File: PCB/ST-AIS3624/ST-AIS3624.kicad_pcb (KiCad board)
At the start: 2 copper layers, 25 x 9 mm, 5 parts, among them J1 Conn_02x03_Odd_Even

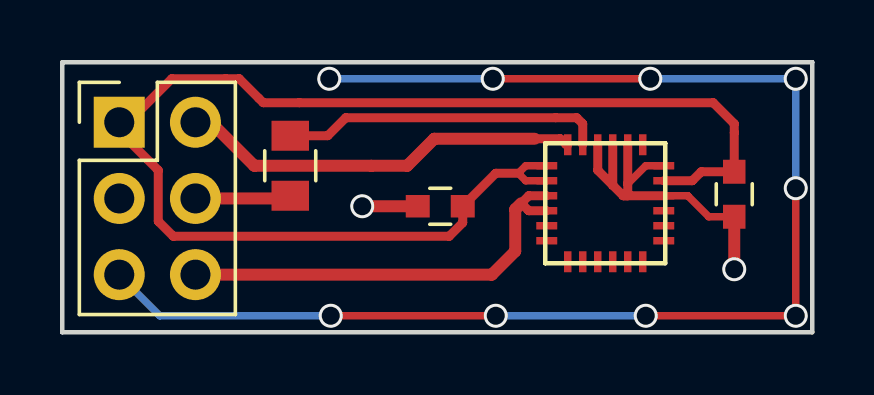
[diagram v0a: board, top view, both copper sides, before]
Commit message: PCB - AIS3624 fix  bad wiring for SPI interface 3-wire
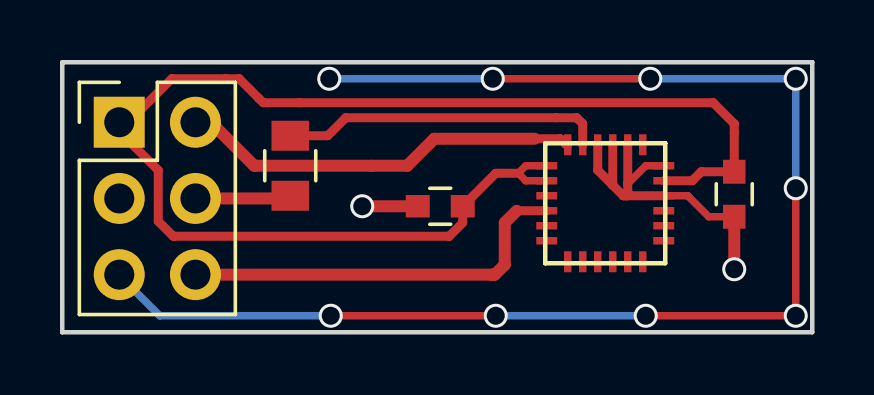
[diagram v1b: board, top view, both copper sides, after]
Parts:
- AIS36241: value Acc1 -> AIS3624DQTR
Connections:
- AIS36241 pad 15: /Miso/Mosi -> Net-(AIS36241-Pad15)
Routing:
- net /Miso/Mosi: track 14.6 -> 13.4 mm
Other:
- board text added: "BI-SDI"
- board text added: "SDO"
- board text removed: "MOSI MISO"
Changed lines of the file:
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@@
 (kicad_pcb (version 4) (host pcbnew 4.0.7)
   (general
-    (links 18)
+    (links 17)
     (no_connects 0)
-    (area 107.214287 61.8 150.785715 90.575)
+    (area 107.214287 61.8 155.5 90.575)
     (thickness 1.6)
-    (drawings 36)
-    (tracks 89)
+    (drawings 40)
+    (tracks 87)
     (zones 0)
     (modules 5)
-    (nets 19)
+    (nets 20)
   )
   (page A4)
@@
     (visible_elements 7FFFF77F)
     (pcbplotparams
-      (layerselection 0x000cc_80000001)
+      (layerselection 0x000c8_80000001)
       (usegerberextensions false)
       (excludeedgelayer true)
@@
   (net 17 "Net-(AIS36241-Pad24)")
   (net 18 "Net-(J1-Pad4)")
+  (net 19 "Net-(AIS36241-Pad15)")
   (net_class Default "Ceci est la Netclass par défaut"
     (clearance 0.2)
@@
     (add_net GNDREF)
     (add_net "Net-(AIS36241-Pad1)")
+    (add_net "Net-(AIS36241-Pad15)")
     (add_net "Net-(AIS36241-Pad17)")
     (add_net "Net-(AIS36241-Pad18)")
@@
       (effects (font (size 1 1) (thickness 0.15)))
     )
-    (fp_text value Acc1 (at 0.6 -2.9 180) (layer F.Fab)
+    (fp_text value AIS3624DQTR (at 0.6 -2.9 180) (layer F.Fab) hide
       (effects (font (size 1 1) (thickness 0.15)))
     )
@@
       (net 5 /VDD))
     (pad 15 smd rect (at 1.95 0.25 180) (size 0.7 0.25) (layers F.Cu F.Paste F.Mask)
-      (net 9 /Miso/Mosi))
+      (net 19 "Net-(AIS36241-Pad15)"))
     (pad 16 smd rect (at 1.95 -0.25 180) (size 0.7 0.25) (layers F.Cu F.Paste F.Mask)
       (net 9 /Miso/Mosi))
@@
     )
   )
+  (target plus (at 117 88) (size 5) (width 0.15) (layer Edge.Cuts))
+  (target plus (at 116 67) (size 5) (width 0.15) (layer Edge.Cuts))
+  (target plus (at 153 67) (size 5) (width 0.15) (layer Edge.Cuts))
+  (gr_text BI-SDI (at 136.8 78) (layer Eco1.User)
+    (effects (font (size 0.3 0.3) (thickness 0.05)))
+  )
   (gr_text VDD (at 143.1 77) (layer Eco1.User)
     (effects (font (size 0.3 0.3) (thickness 0.075)))
   )
-  (gr_text VDD (at 137 76.7) (layer Eco1.User)
+  (gr_text VDD (at 137.1 76.7) (layer Eco1.User)
     (effects (font (size 0.3 0.3) (thickness 0.075)))
   )
@@
     (effects (font (size 0.3 0.3) (thickness 0.075)))
   )
-  (gr_text "MOSI\nMISO" (at 136.9 77.8) (layer Eco1.User)
+  (gr_text "SDO\n" (at 137.1 77.5) (layer Eco1.User)
     (effects (font (size 0.3 0.3) (thickness 0.075)))
   )
@@
   (segment (start 134.4 75.55) (end 137.75 75.55) (width 0.4) (layer F.Cu) (net 8))
   (segment (start 133.5 76.45) (end 134.4 75.55) (width 0.4) (layer F.Cu) (net 8))
-  (segment (start 137.1 79.3) (end 137.1 77.9) (width 0.4) (layer F.Cu) (net 9))
-  (segment (start 136.32 80.08) (end 137.1 79.3) (width 0.4) (layer F.Cu) (net 9))
+  (segment (start 136.32 80.08) (end 136.42 80.08) (width 0.4) (layer F.Cu) (net 9))
   (segment (start 126.44 80.08) (end 136.32 80.08) (width 0.4) (layer F.Cu) (net 9))
-  (segment (start 137.1 77.9) (end 137.3 77.7) (width 0.4) (layer F.Cu) (net 9))
-  (segment (start 137.3 77.7) (end 137.55 77.95) (width 0.3) (layer F.Cu) (net 9))
-  (segment (start 137.55 77.45) (end 137.3 77.7) (width 0.3) (layer F.Cu) (net 9))
-  (segment (start 138.15 77.45) (end 137.55 77.45) (width 0.3) (layer F.Cu) (net 9))
-  (segment (start 137.55 77.95) (end 138.15 77.95) (width 0.3) (layer F.Cu) (net 9))
+  (segment (start 137.15 77.95) (end 138.15 77.95) (width 0.3) (layer F.Cu) (net 9))
+  (segment (start 136.75 78.35) (end 137.15 77.95) (width 0.4) (layer F.Cu) (net 9))
+  (segment (start 136.75 79.75) (end 136.75 78.35) (width 0.4) (layer F.Cu) (net 9))
+  (segment (start 136.42 80.08) (end 136.75 79.75) (width 0.4) (layer F.Cu) (net 9))
   (segment (start 126.44 77.54) (end 129.51 77.54) (width 0.4) (layer F.Cu) (net 18))
   (segment (start 129.51 77.54) (end 129.6 77.45) (width 0.25) (layer F.Cu) (net 18))
